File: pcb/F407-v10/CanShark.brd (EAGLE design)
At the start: 97 x 80 mm, 135 parts, among them IC1 STM32F407V, IC2 KSZ8051MLL, K2 JACK_POWER_2,1, U1 SN65HVD230DR, U2 SN65HVD230DR, U3 LM2594M-ADJ, U4 LM2594M-ADJ, U5 TSH24IDT, U6 MCP602-E/SN

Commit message: remove JTAG connector,
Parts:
- removed JP6: (no value), pinhead:2X10
- removed R36: 10k, #Odpory:R0603
- removed R39, R40: 100k, #Odpory:R0603
- moved LED1 130.4 mm to (54.2, 53.2), turned to 180 degrees
- moved R43 127.6 mm to (50.8, 53.2), turned to 180 degrees
- moved R41 113.8 mm to (18.2, 38.1)
- moved R38 102.1 mm to (18.2, 32.9)
- moved R37 100.3 mm to (18.3, 27.7), turned to 180 degrees
- moved R42 86.5 mm to (18.3, 25.1)
- moved C33 32.5 mm to (40.9, 54.0)
- moved C34 32.5 mm to (44.1, 41.7)
- moved R60 32.5 mm to (40.0, 41.7)
- moved R61 32.5 mm to (42.0, 41.7)
- moved R62 32.5 mm to (46.1, 41.7)
- moved U6 32.5 mm to (41.9, 48.5)
- moved JP7 30.6 mm to (22.1, 31.6), turned to 90 degrees
- moved R55 18.8 mm to (32.1, 59.6), turned to 0 degrees
- moved R57 17.7 mm to (36.4, 55.8), turned to 0 degrees
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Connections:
- removed net N$8: JP6.11, R36.1
- net +3V3: no longer JP6.1, JP6.2, R39.1, R40.1
- net GND: no longer JP6.10, JP6.12, JP6.14, JP6.16, JP6.18, JP6.20, JP6.4, JP6.6, JP6.8, R36.2
- net JTG-TCK/SWCLK: no longer JP6.9
- net JTG-TDI: no longer JP6.5, R39.2
- net JTG-TDO/SWO: no longer JP6.13
- net JTG-TMS/SWDIO: no longer JP6.7
- net JTG-TRST: no longer JP6.3, R40.2
- net NRST: no longer JP6.15
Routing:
- net JTG-TDO/SWO: track 0.00 -> 31.7 mm
- net NRST: track 9.55 -> 37.9 mm
- net +3V3: track 191.7 -> 211.4 mm
- net GND: track 242.1 -> 231.0 mm
- net JTG-TCK/SWCLK: track 0.00 -> 8.74 mm
- net JTG-TMS/SWDIO: track 0.00 -> 3.09 mm
- net N$27: track 0.00 -> 3.01 mm
- net N$4: track 7.35 -> 4.36 mm
- net V+: track 22.6 -> 25.3 mm
- net N$35: track 0.00 -> 1.83 mm

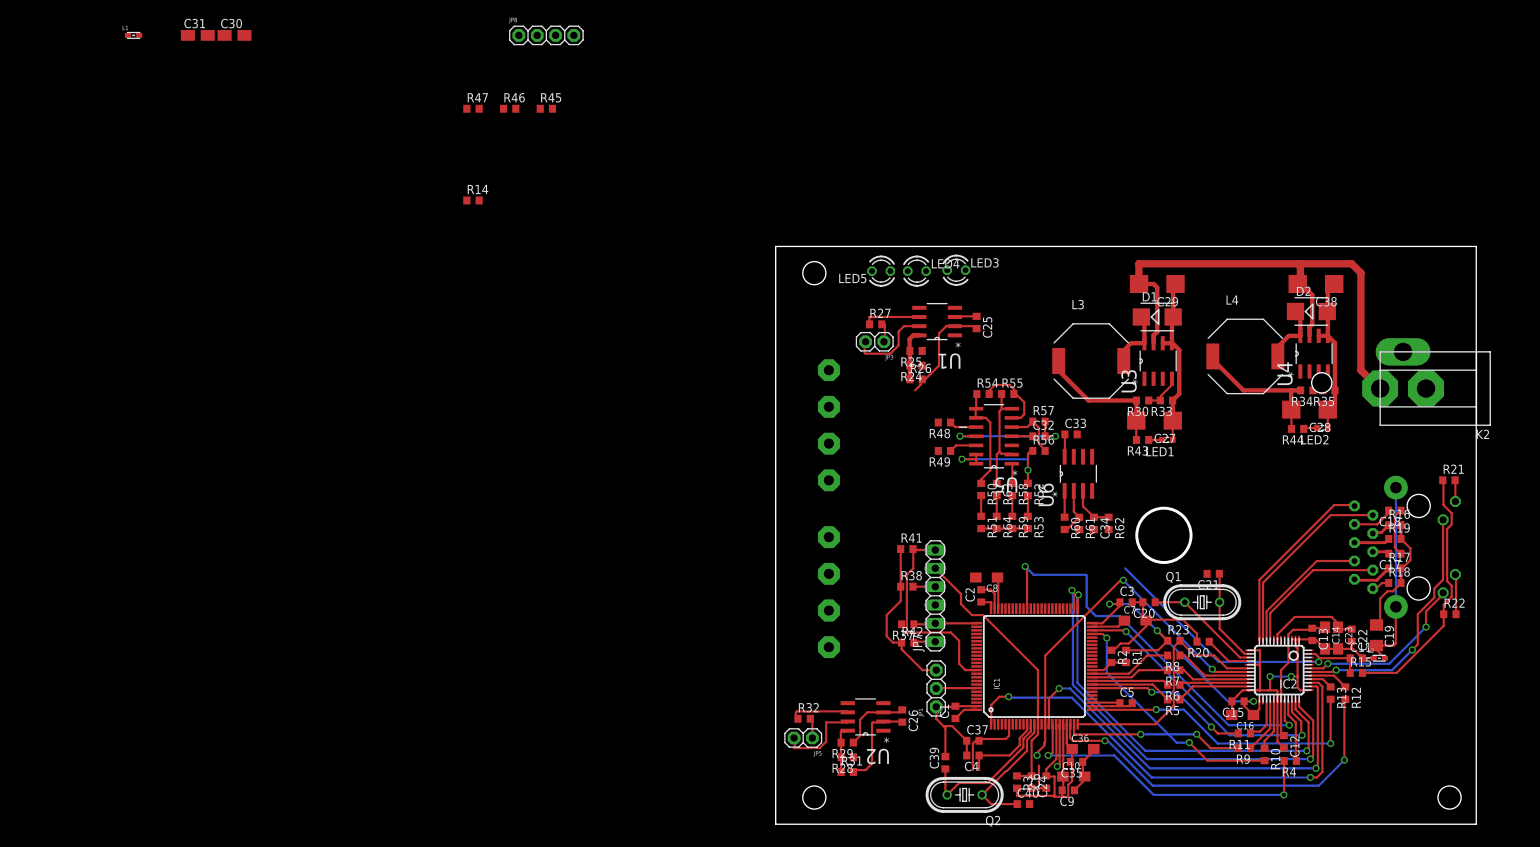
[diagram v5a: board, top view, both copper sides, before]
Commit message: Change LED, ETH RST and INTRPT pins on processor
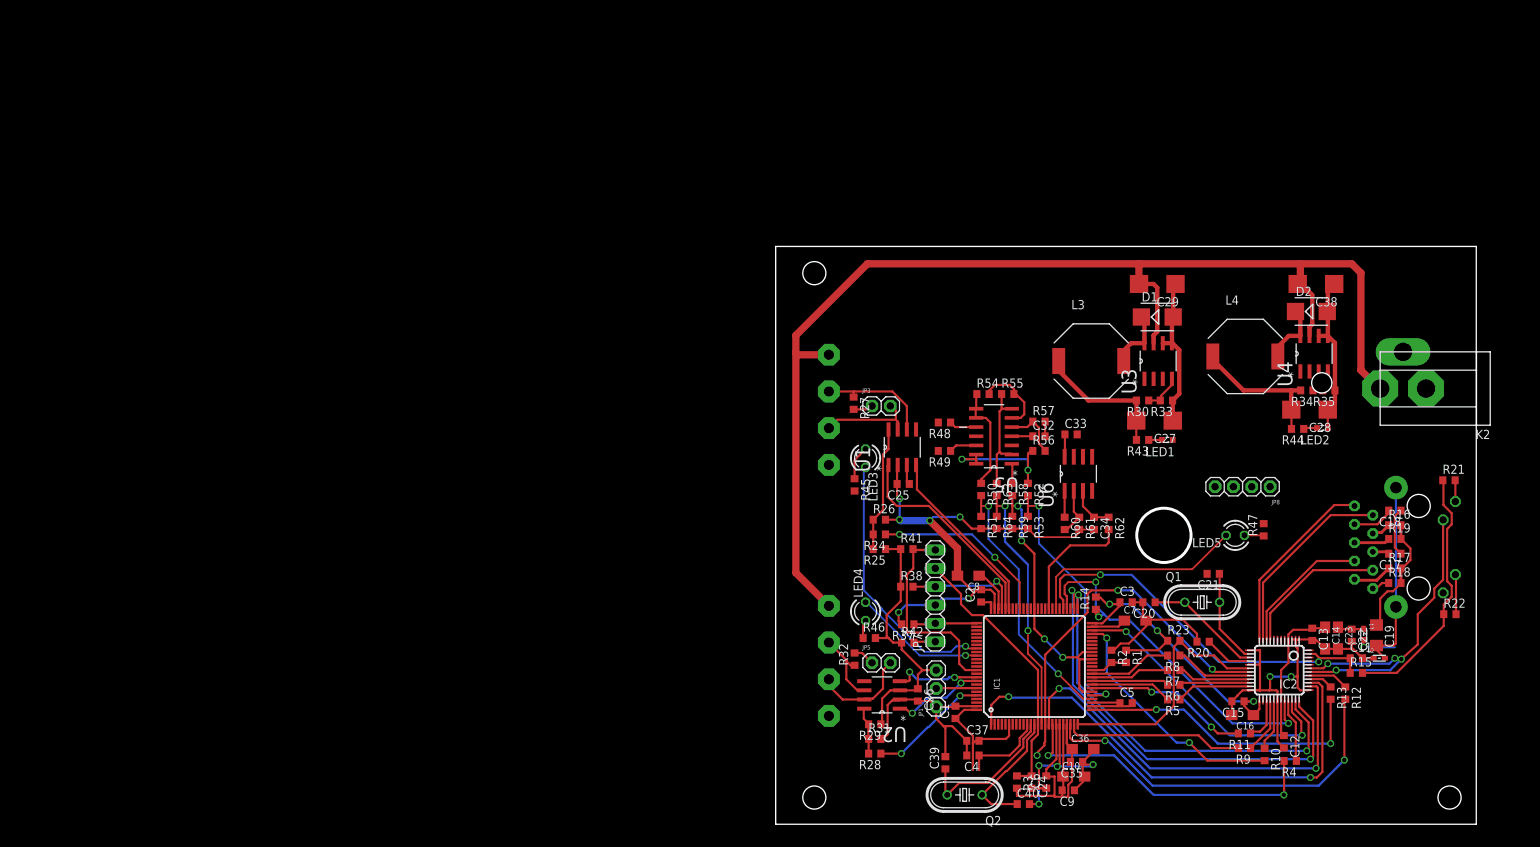
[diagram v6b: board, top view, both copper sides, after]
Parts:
- removed C30, C31: (no value), rcl:A/3216-18R
- moved L1 189.4 mm to (81.4, 26.3), turned to 270 degrees
- moved R47 124.0 mm to (67.6, 40.8), turned to 90 degrees
- moved JP8 114.9 mm to (64.6, 46.7), turned to 180 degrees
- moved R14 102.7 mm to (44.3, 30.6), turned to 90 degrees
- moved R46 88.6 mm to (13.0, 25.8)
- moved R45 67.3 mm to (10.9, 47.0), turned to 270 degrees
- moved LED5 61.2 mm to (63.6, 40.0)
- moved LED4 47.7 mm to (12.4, 29.5), turned to 90 degrees
- moved LED3 28.9 mm to (12.4, 50.7), turned to 270 degrees
- moved R25 27.9 mm to (14.4, 38.1)
- moved C25 24.6 mm to (17.7, 47.1), turned to 180 degrees
- moved R24 23.9 mm to (14.4, 40.1)
- moved R26 20.1 mm to (14.4, 42.2)
- moved U1 18.1 mm to (17.5, 52.2), turned to 90 degrees
- moved JP5 15.0 mm to (14.6, 22.4), turned to 0 degrees
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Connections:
- net CAN2_MODE: now also IC1.96; no longer IC1.66
- net ETH_INTRP: now also IC1.54; no longer IC1.65
- net ETH_RST: now also IC1.55; no longer IC1.64
- net EXTSUPPLY: no longer C30.+
- net GND: no longer C30.-, C31.-
- net LED_CAN1: now also IC1.83; no longer IC1.55
- net LED_CAN2: now also IC1.85; no longer IC1.56
- net V+: no longer C31.+
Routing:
- net EXTSUPPLY: track 73.5 -> 169.3 mm
- net GND: track 231.0 -> 270.9 mm, vias 4 -> 12
- net ADC_TRIG: track 2.87 -> 39.7 mm, vias 0 -> 4
- net LED_CAN1: track 0.00 -> 36.8 mm, vias 0 -> 1
- net ADC_CAN1L: track 2.87 -> 37.3 mm, vias 0 -> 2
- net ADC_CAN1H: track 2.87 -> 37.1 mm, vias 0 -> 2
- net ADC_CAN1DIFF: track 2.87 -> 36.3 mm, vias 0 -> 2
- net LED_GLOBAL: track 0.00 -> 30.3 mm
- net CAN1_TX: track 0.00 -> 29.3 mm
- net CAN1_RX: track 0.00 -> 26.0 mm
- net CAN1_MODE: track 0.00 -> 25.0 mm, vias 0 -> 2
- net LED_CAN2: track 0.00 -> 18.4 mm, vias 0 -> 1
- net +3V3: track 211.4 -> 229.1 mm, vias 3 -> 4
- net ADC_TRIG_VALUE_PWM: track 0.00 -> 17.3 mm
- net CAN2_MODE: track 0.00 -> 16.6 mm, vias 0 -> 2
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
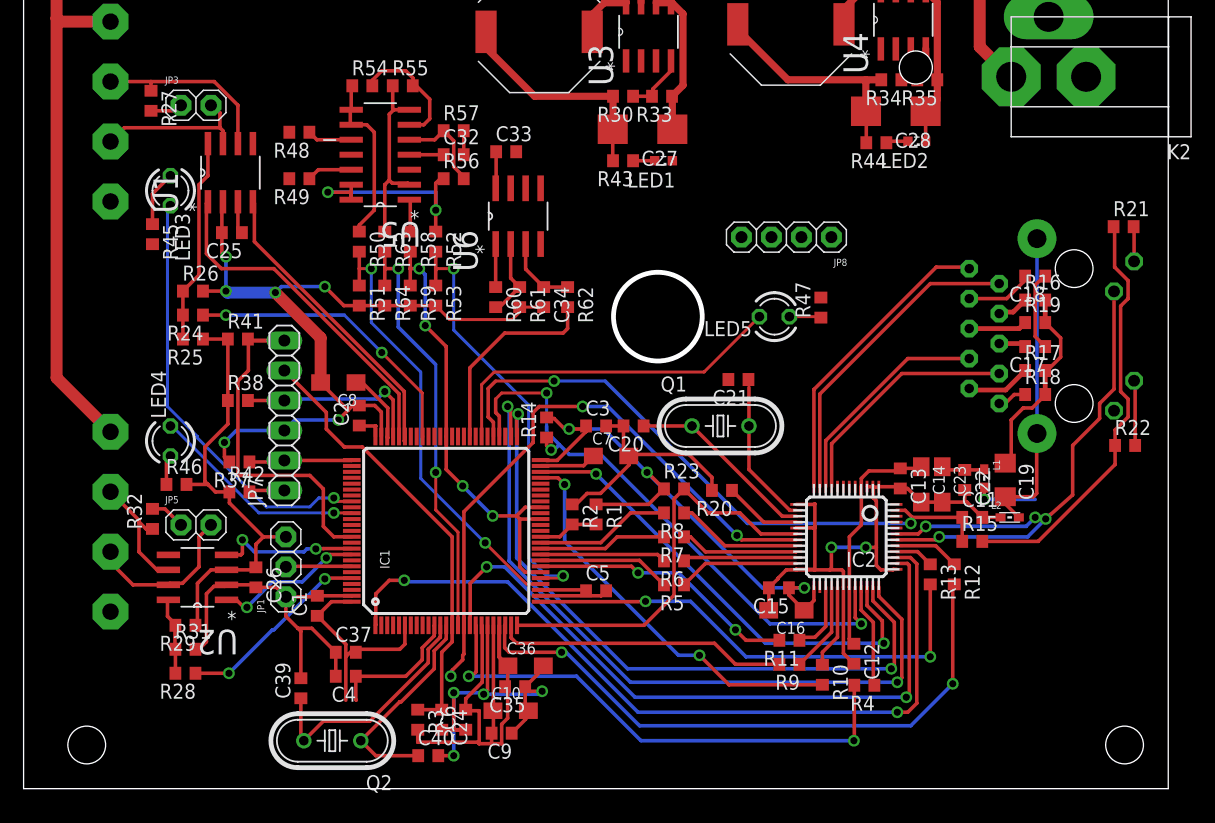
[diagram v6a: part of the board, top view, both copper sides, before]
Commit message: Change debug USART, finish routing
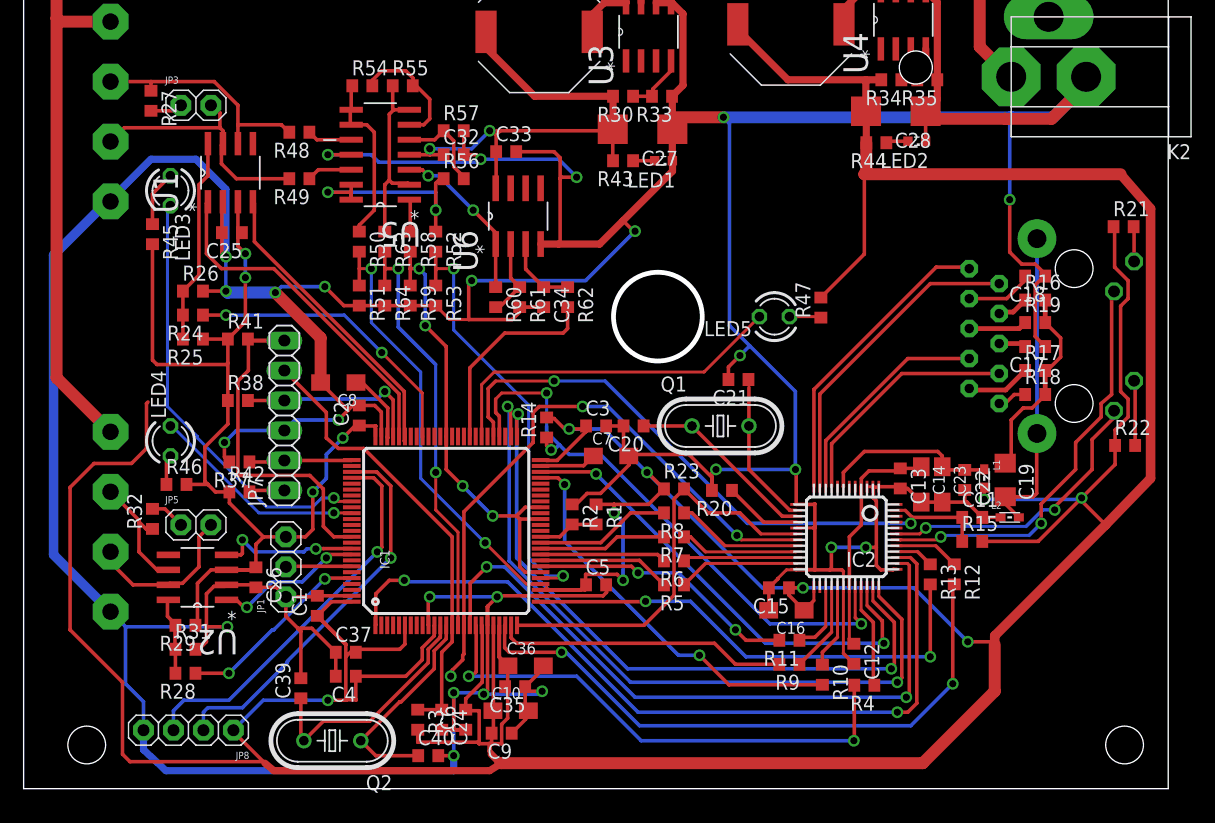
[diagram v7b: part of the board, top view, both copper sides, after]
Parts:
- moved JP8 65.7 mm to (14.0, 4.95)
- moved C5 0.51 mm to (48.5, 17.3)
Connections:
- removed net N$3: C5.1, IC1.28
- removed net USART1_RX: IC1.69, JP8.3
- removed net USART1_TX: IC1.68, JP8.2
- new net USART3_RX: IC1.79, JP8.3
- new net USART3_TX: IC1.78, JP8.2
- net +3V3: now also C5.1, IC1.28
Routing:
- net GND: track 270.9 -> 592.8 mm, vias 12 -> 25
- net +3V3: track 229.1 -> 537.8 mm, vias 4 -> 13
- net USART3_RX: track 0.00 -> 33.1 mm, vias 0 -> 1
- net USART3_TX: track 0.00 -> 32.8 mm, vias 0 -> 1
- net V+: track 25.3 -> 43.9 mm, vias 0 -> 2
- net N$51: track 12.5 -> 24.9 mm
- net N$9: track 3.69 -> 15.1 mm
- net N$68: track 3.65 -> 14.1 mm, vias 0 -> 2
- net CAN1_H: track 13.5 -> 21.5 mm
- net CAN1_L: track 15.7 -> 20.3 mm
- net N$3: track 3.88 -> 0.00 mm
- net N$50: track 35.7 -> 35.1 mm

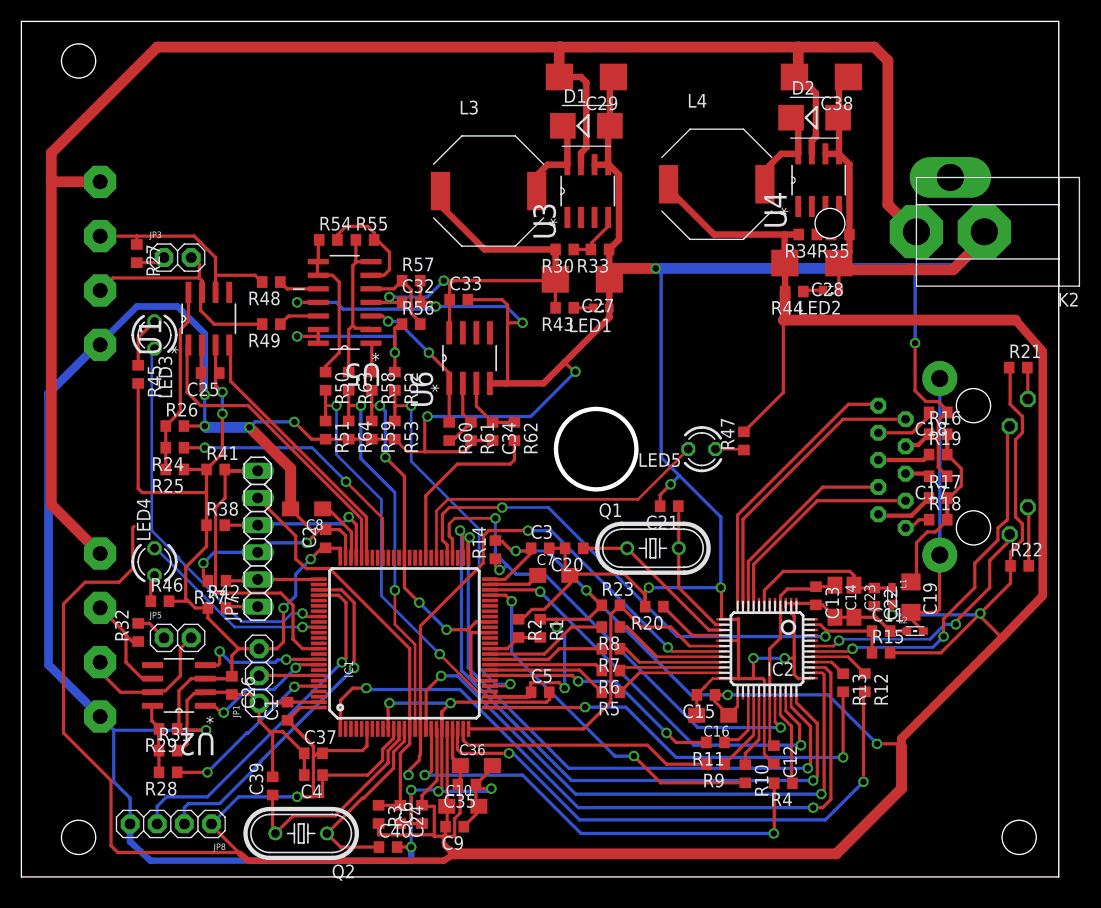
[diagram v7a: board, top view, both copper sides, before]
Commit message: add GND polygon
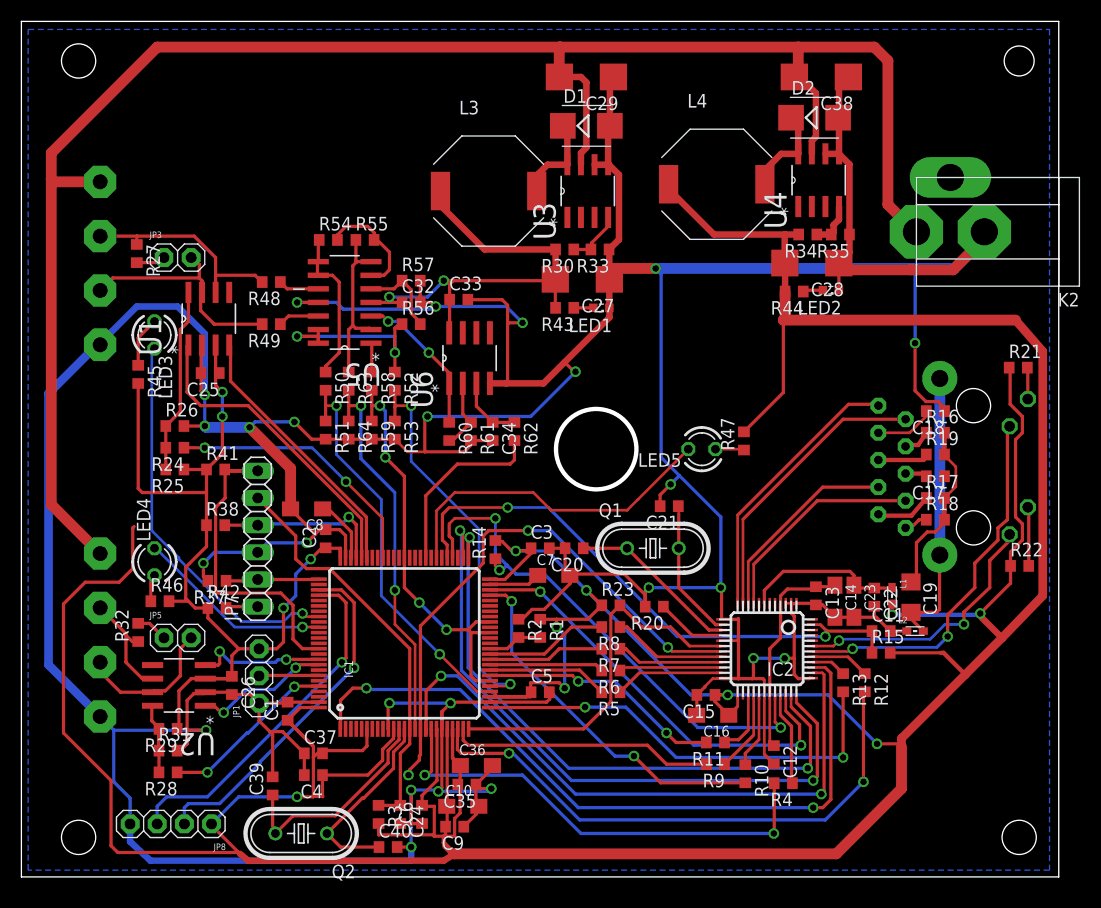
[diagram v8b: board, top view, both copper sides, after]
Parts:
- moved C18 0.28 mm to (85.5, 43.6)
- moved R16 0.28 mm to (85.5, 41.5)
- moved C17 0.25 mm to (85.5, 37.5)
- moved R17 0.25 mm to (85.5, 35.4)
- moved R18 0.25 mm to (85.5, 33.4)
- moved R19 0.25 mm to (85.5, 39.5)
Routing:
- net GND: track 592.8 -> 586.4 mm
- net +3V3: track 537.8 -> 535.7 mm
- net LED_GLOBAL: track 30.3 -> 31.7 mm
- added copper zone on layer 16, net GND
